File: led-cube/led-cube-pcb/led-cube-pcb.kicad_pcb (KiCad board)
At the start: 2 copper layers, 100 x 80 mm, 26 parts, among them J1 9V, J2 LED Cube, Q1 LW_PMOS, Q2 LW_PMOS, Q3 LW_PMOS, SW1 LW_Tactile_Switch, U1 Pi Pico, U2 7805, U3 ULN2003A, U4 ULN2003A

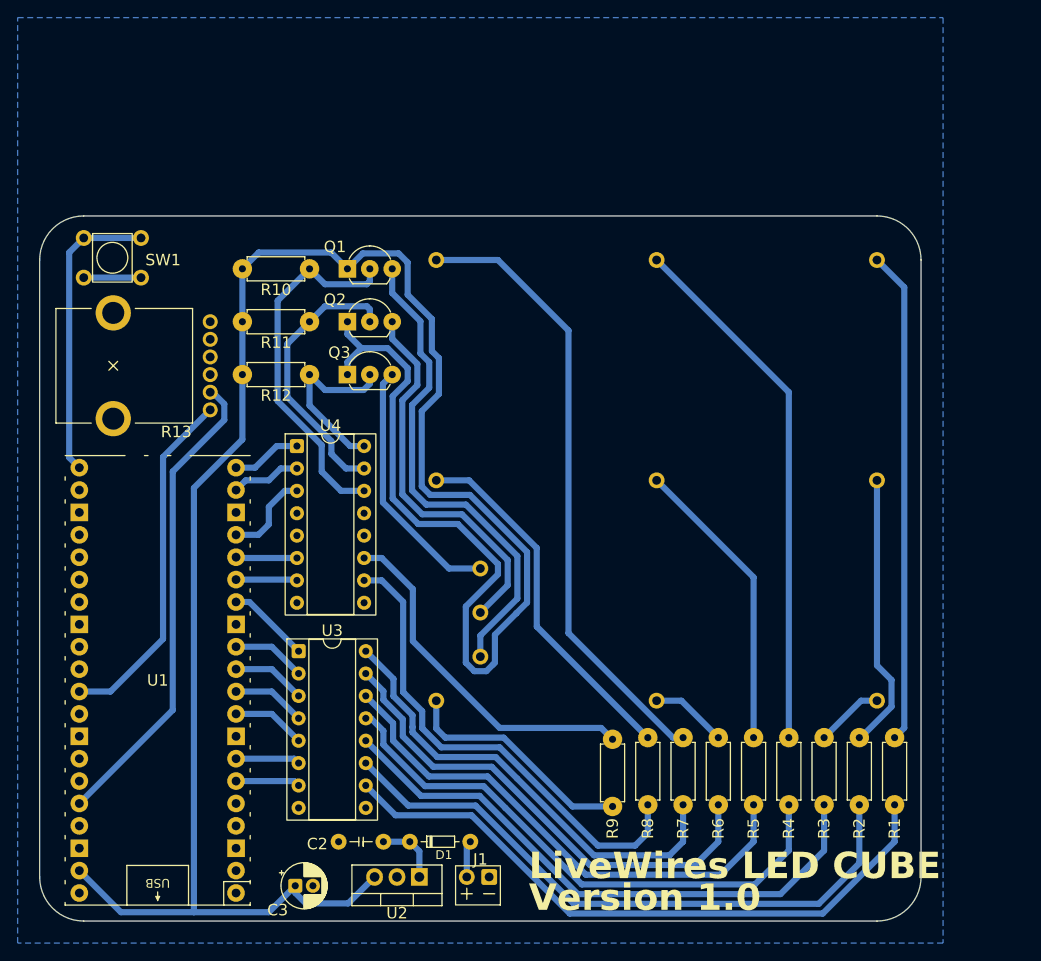
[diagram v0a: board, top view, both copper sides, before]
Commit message: Released v1.1 of the LED cube PCB, with better LED spacing and some convenience features
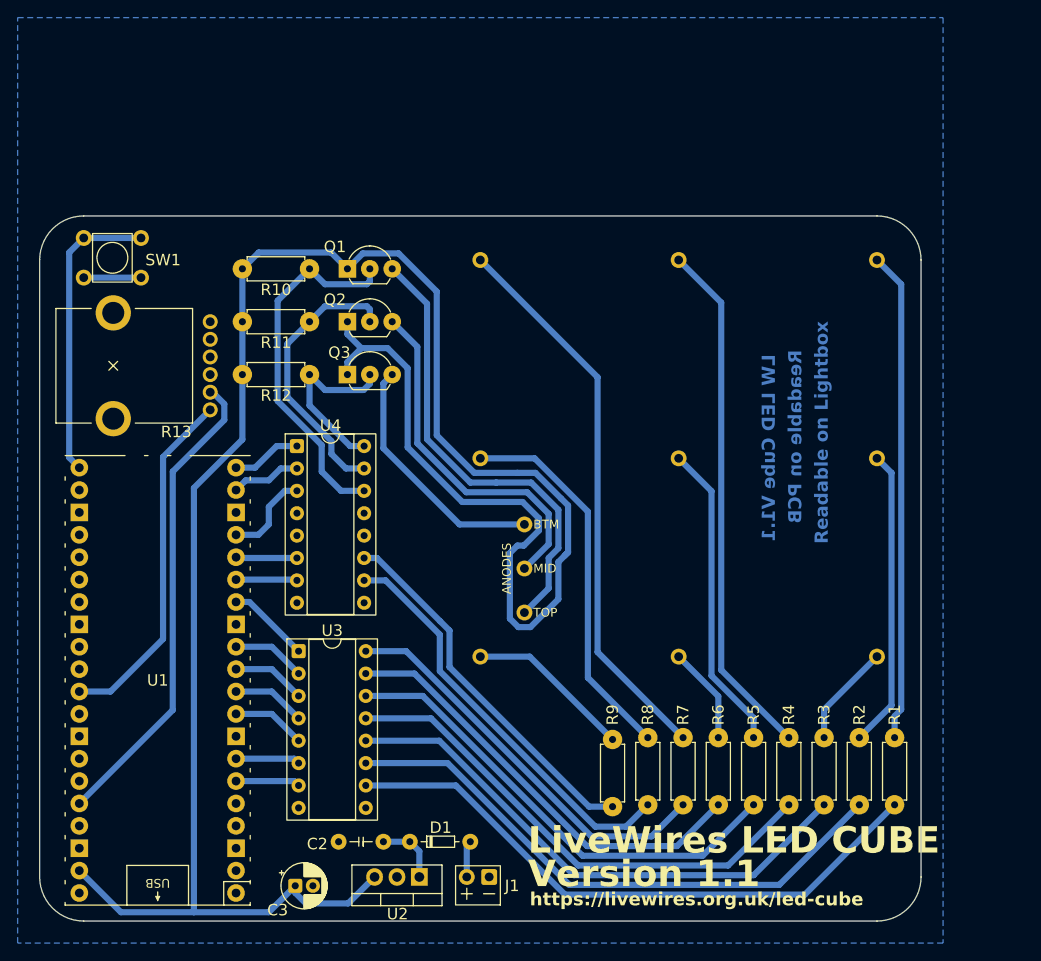
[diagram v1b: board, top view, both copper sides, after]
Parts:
- moved R9 7.64 mm to (165.0, 137.0), turned to 90 degrees
- moved J2 7.07 mm to (150.0, 120.0)
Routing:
- net Net-(U4-OUT7): track 55.6 -> 47.2 mm
- net Net-(J2-C1): track 26.8 -> 18.9 mm
- net Net-(J2-C3): track 70.6 -> 63.7 mm
- net Net-(U3-OUT1): track 52.7 -> 46.2 mm
- net Net-(U3-OUT2): track 56.0 -> 50.0 mm
- net Net-(U3-OUT4): track 63.5 -> 57.8 mm
- net +5V: track 253.6 -> 247.9 mm
- net Net-(U3-OUT6): track 71.2 -> 65.5 mm
- net Net-(U3-OUT3): track 59.3 -> 53.9 mm
- net Net-(U3-OUT5): track 66.4 -> 61.6 mm
- net Net-(U3-OUT7): track 73.6 -> 69.3 mm
- net Net-(J2-C7): track 7.74 -> 11.7 mm
- net Net-(J2-A1): track 55.9 -> 52.4 mm
- net Net-(J2-A2): track 43.8 -> 40.5 mm
- net Net-(J2-C8): track 31.5 -> 33.9 mm
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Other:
- board text added: "LW LED Cube V1.1"
- board text added: "Readable on Lightbox"
- board text added: "Readable on PCB"
- board text added: "Version 1.1"
- board text added: "https://livewires.org.uk/led-cube"
- board text removed: "Version 1.0"
